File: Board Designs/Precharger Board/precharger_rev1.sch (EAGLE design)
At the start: 19 parts, among them X1 CONNECTOR-2, X2 CONNECTOR-2

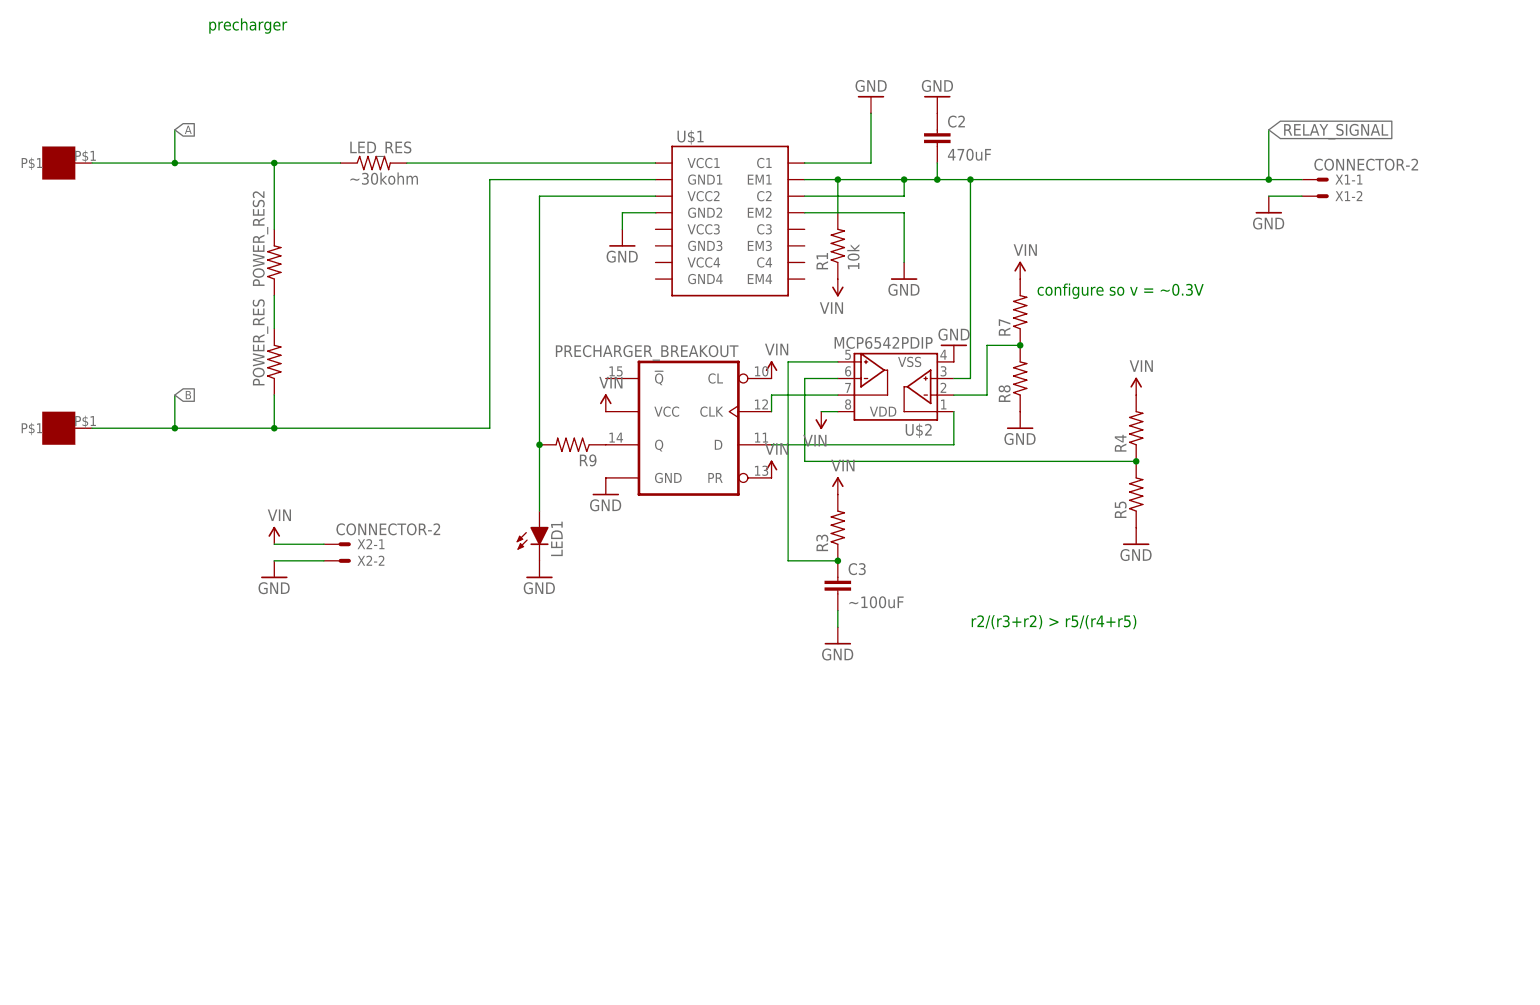
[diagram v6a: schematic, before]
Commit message: Revised precharger design
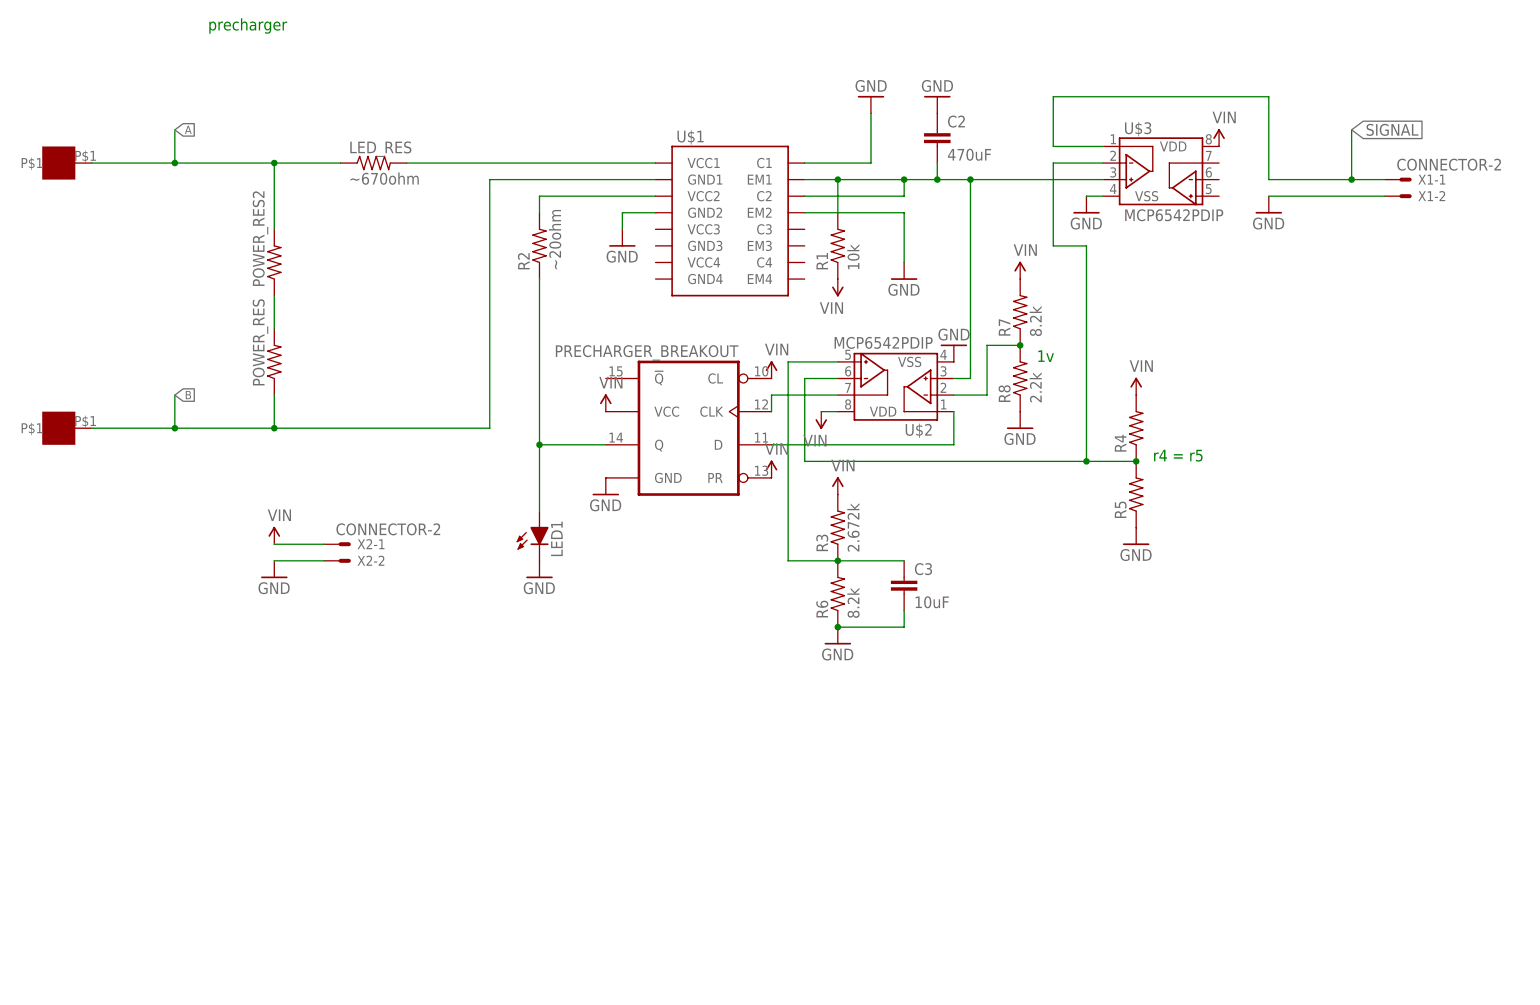
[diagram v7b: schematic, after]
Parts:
- removed R9: (no value), HyTechDevices:RESISTORAXIAL-0.3
- added R2: ~20ohm, HyTechDevices:RESISTORAXIAL-0.3
- added R6: 8.2k, HyTechDevices:RESISTORAXIAL-0.3
- added U$3: MCP6542PDIP, HyTechDevices:MCP6542PDIP
- C3: value ~100uF -> 10uF
- LED_RES: value ~30kohm -> ~670ohm
- R3: value (none) -> 2.672k
- R7: value (none) -> 8.2k
- R8: value (none) -> 2.2k
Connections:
- removed net N$7: LED1.A, R9.2, U$1.VCC2
- removed net N$8: C3.1, R3.1, U$2.VINB+
- removed net RELAY_SIGNAL: C2.2, R1.2, U$1.C2, U$1.EM1, U$2.VINA+, X1-1.S
- new net N$12: R2.2, U$1.VCC2
- new net N$3: C3.1, R6.2, U$2.VINB+
- new net NODE: C2.2, R1.2, U$1.C2, U$1.EM1, U$2.VINA+, U$3.VINA+
- new net SIGNAL: U$3.VOUTA, X1-1.S
- net GND: now also R6.1, U$3.VSS
- net N$1: now also LED1.A, R2.1; no longer R9.1
- net N$10: now also U$3.VINA-
- net VIN: now also U$3.VDD
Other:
- note added: "1v"
- note added: "r4 = r5"
- note removed: "configure so v = ~0.3V"
- note removed: "r2/(r3+r2) > r5/(r4+r5)"
- moved on the sheet: C3, X1-1, X1-2

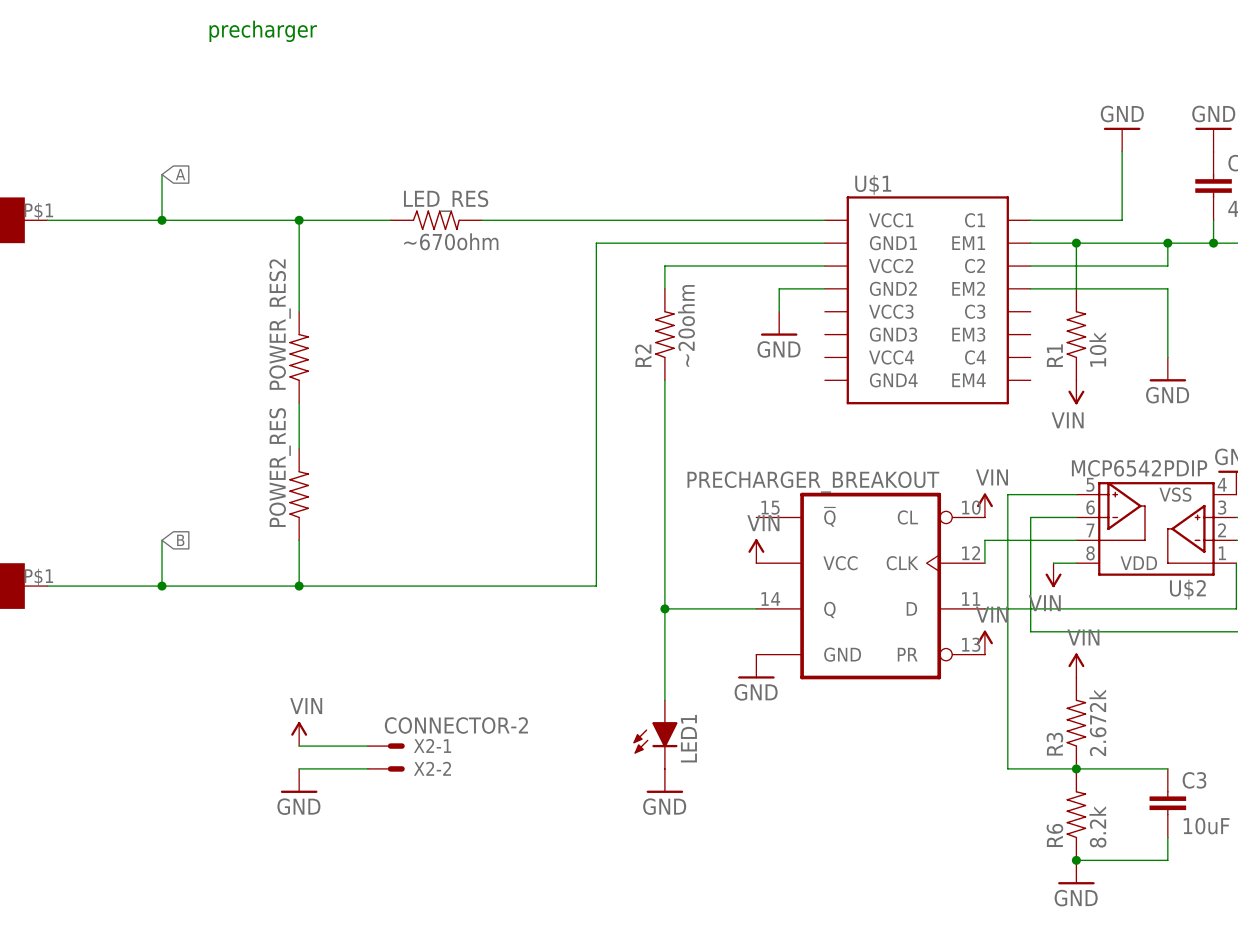
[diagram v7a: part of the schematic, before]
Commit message: Revised Precharger Design
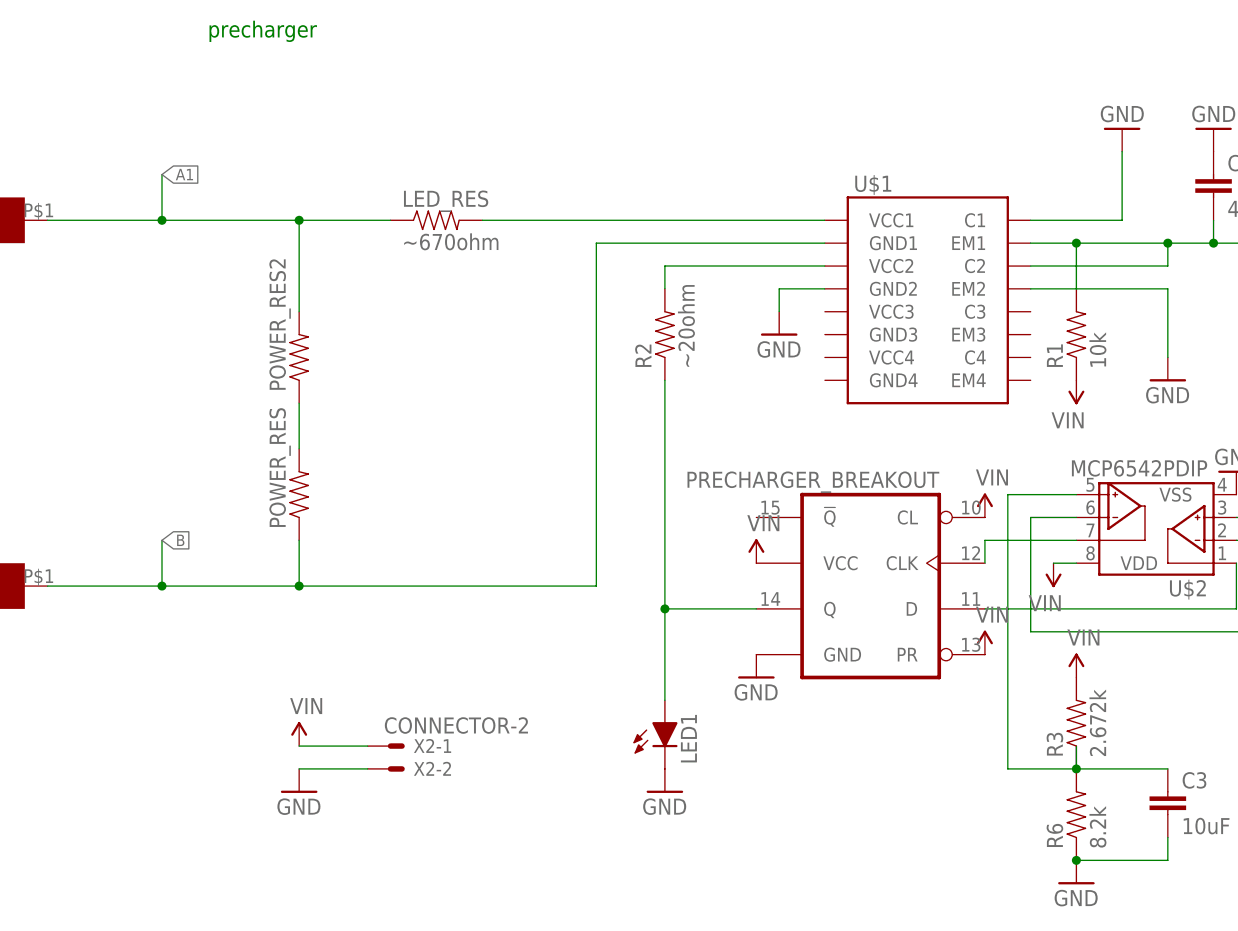
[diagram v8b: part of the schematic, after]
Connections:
- net A renamed A1
- net N$3: now also R3.1
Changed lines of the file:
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@@
 </segment>
 </net>
-<net name="A" class="0">
+<net name="A1" class="0">
 <segment>
 <pinref part="LED_RES" gate="G$1" pin="1"/>
 <wire x1="106.68" y1="78.74" x2="96.52" y2="78.74" width="0.1524" layer="91"/>
+<pinref part="POWER_RES2" gate="G$1" pin="2"/>
+<wire x1="96.52" y1="68.58" x2="96.52" y2="78.74" width="0.1524" layer="91"/>
+<junction x="96.52" y="78.74"/>
+<pinref part="+" gate="G$1" pin="P$1"/>
+<wire x1="81.28" y1="78.74" x2="81.28" y2="83.82" width="0.1524" layer="91"/>
+<wire x1="81.28" y1="78.74" x2="68.58" y2="78.74" width="0.1524" layer="91"/>
 <label x="81.28" y="83.82" size="1.27" layer="95" xref="yes"/>
 <wire x1="96.52" y1="78.74" x2="81.28" y2="78.74" width="0.1524" layer="91"/>
-<wire x1="81.28" y1="78.74" x2="81.28" y2="83.82" width="0.1524" layer="91"/>
-<junction x="96.52" y="78.74"/>
-<pinref part="POWER_RES2" gate="G$1" pin="2"/>
-<wire x1="96.52" y1="68.58" x2="96.52" y2="78.74" width="0.1524" layer="91"/>
-<pinref part="+" gate="G$1" pin="P$1"/>
-<wire x1="81.28" y1="78.74" x2="68.58" y2="78.74" width="0.1524" layer="91"/>
 <junction x="81.28" y="78.74"/>
 </segment>
@@
 <pinref part="R6" gate="G$1" pin="2"/>
 <junction x="182.88" y="17.78"/>
-</segment>
-</net>
+<pinref part="R3" gate="G$1" pin="1"/>
+<wire x1="182.88" y1="20.32" x2="182.88" y2="17.78" width="0.1524" layer="91"/>
+</segment>
+</net>
